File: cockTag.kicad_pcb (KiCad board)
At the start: 4 copper layers, 25 x 25 mm, 46 parts, among them J1 SWD, Q1 Q_NPN_BEC, U1 KXTJ3-1057, U2 nRF51x22-QFxx, Y1 32.768kHz, Y2 16MHz

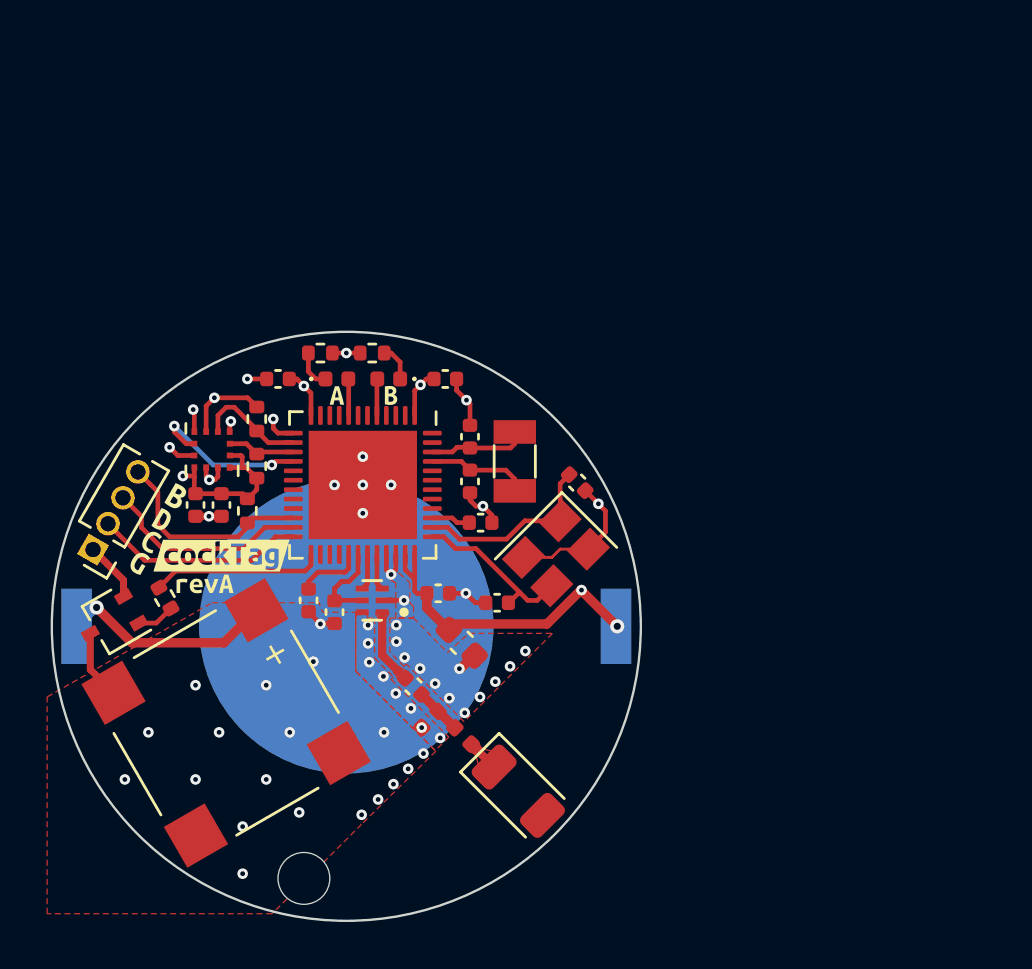
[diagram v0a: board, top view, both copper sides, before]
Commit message: Change schematic to NRF52832
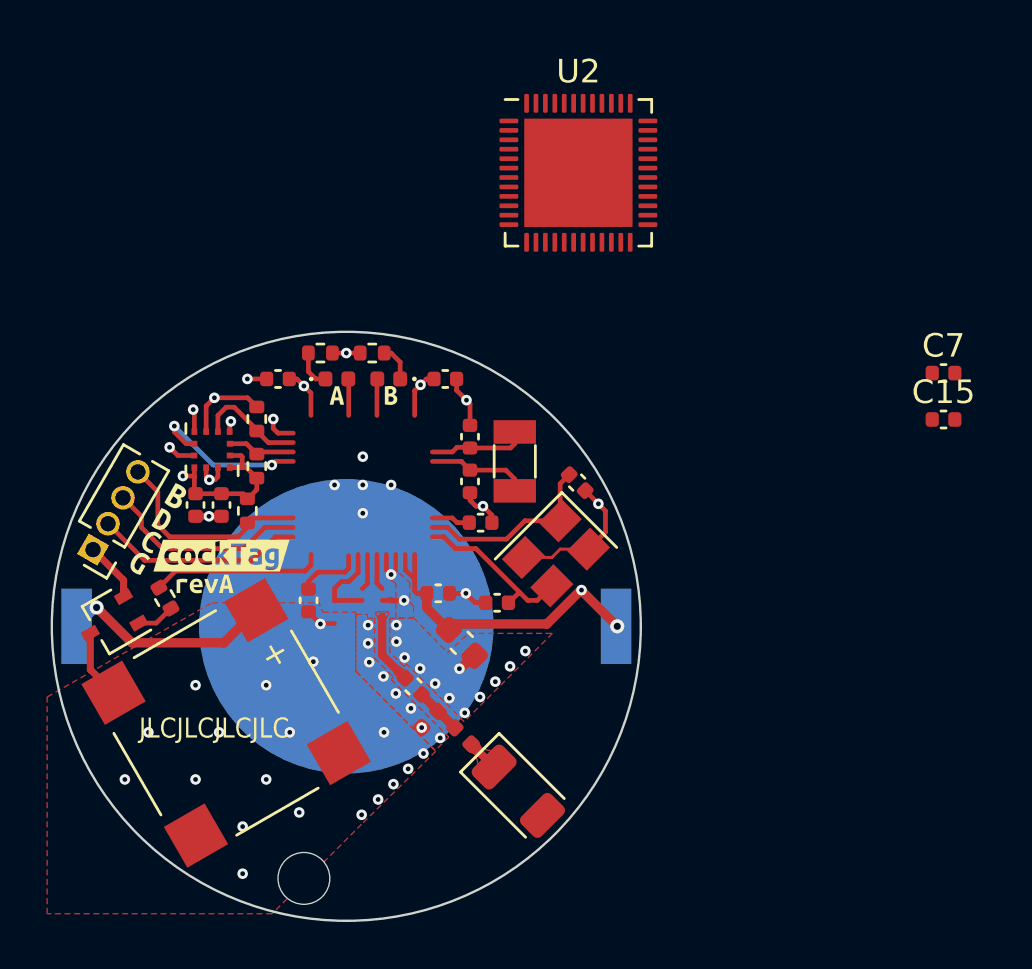
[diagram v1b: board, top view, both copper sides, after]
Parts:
- removed B1: nRF-BALUN, Library:FIL_2450BM14E0003T
- added C15: 100p, Capacitor_SMD:C_0402_1005Metric, F.Cu at (175.6, 91.2)
- C4: value 47n -> 100p
- C7: value 47n -> 1u
- U2: value nRF51x22-QFxx -> nRF52832-QFxx
- moved C7 27.8 mm to (175.6, 89.2), turned to 0 degrees
- moved U2 16.1 mm to (160.1, 80.8), turned to 0 degrees
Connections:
- C7 pad 1: VDD_PA -> GND
- C7 pad 2: GND -> Net-(C7-Pad2)
- U2 pad 1: VCC -> Net-(C5-Pad1)
- U2 pad 10: unconnected-(U2-Pad10) -> GYRO_SDA
- U2 pad 11: unconnected-(U2-Pad11) -> GYRO_SCL
- U2 pad 12: VCC -> GYRO_INT
- U2 pad 13: GND -> VCC
- U2 pad 14: GYRO_SDA -> unconnected-(U2-Pad14)
- U2 pad 15: GYRO_SCL -> unconnected-(U2-Pad15)
- U2 pad 16: GYRO_INT -> unconnected-(U2-Pad16)
- U2 pad 19: unconnected-(U2-Pad19) -> BOOT
- U2 pad 2: unconnected-(U2-Pad2) -> XL1
- U2 pad 20: unconnected-(U2-Pad20) -> /MCU + RF/BUZZER
- U2 pad 22: BOOT -> unconnected-(U2-Pad22)
- U2 pad 23: SWDIO -> unconnected-(U2-Pad23)
- U2 pad 24: SWDCLK -> unconnected-(U2-Pad24)
- U2 pad 25: /MCU + RF/BUZZER -> SWDIO
- U2 pad 26: unconnected-(U2-Pad26) -> SWDCLK
- U2 pad 27: unconnected-(U2-Pad27) -> /MCU + RF/LED_A
- U2 pad 29: Net-(C4-Pad2) -> /MCU + RF/LED_B
- U2 pad 3: unconnected-(U2-Pad3) -> XL2
- U2 pad 30: VDD_PA -> /MCU + RF/ANT
- U2 pad 31: /MCU + RF/ANT1 -> GND
- U2 pad 32: /MCU + RF/ANT2 -> Net-(C4-Pad2)
- U2 pad 33: GND -> Net-(C15-Pad2)
- U2 pad 34: GND -> /MCU + RF/XC1
- U2 pad 35: VCC -> /MCU + RF/XC2
- U2 pad 37: /MCU + RF/XC1 -> unconnected-(U2-Pad37)
- U2 pad 38: /MCU + RF/XC2 -> unconnected-(U2-Pad38)
- U2 pad 39: Net-(C5-Pad1) -> unconnected-(U2-Pad39)
- U2 pad 45: XL2 -> GND
- U2 pad 46: XL1 -> Net-(C7-Pad2)
- U2 pad 48: unconnected-(U2-Pad48) -> VCC
- U2 pad 5: /MCU + RF/LED_B -> unconnected-(U2-Pad5)
- U2 pad 8: /MCU + RF/LED_A -> unconnected-(U2-Pad8)
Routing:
- net unconnected-(U2-Pad16): track 0.00 -> 3.75 mm
- net VDD_PA: track 3.75 -> 0.00 mm
- net unconnected-(U2-Pad18): track 0.00 -> 1.54 mm
- net unconnected-(U2-Pad17): track 0.00 -> 1.54 mm
- net /MCU + RF/ANT2: track 1.54 -> 0.00 mm
- net /MCU + RF/ANT1: track 1.54 -> 0.00 mm
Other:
- board text added: "JLCJLCJLCJLC"
